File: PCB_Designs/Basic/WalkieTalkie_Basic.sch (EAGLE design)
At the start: 35 parts, among them Q1 MOSFET-NCHANNELBSS123LT1G, U1 ATMEGA328P

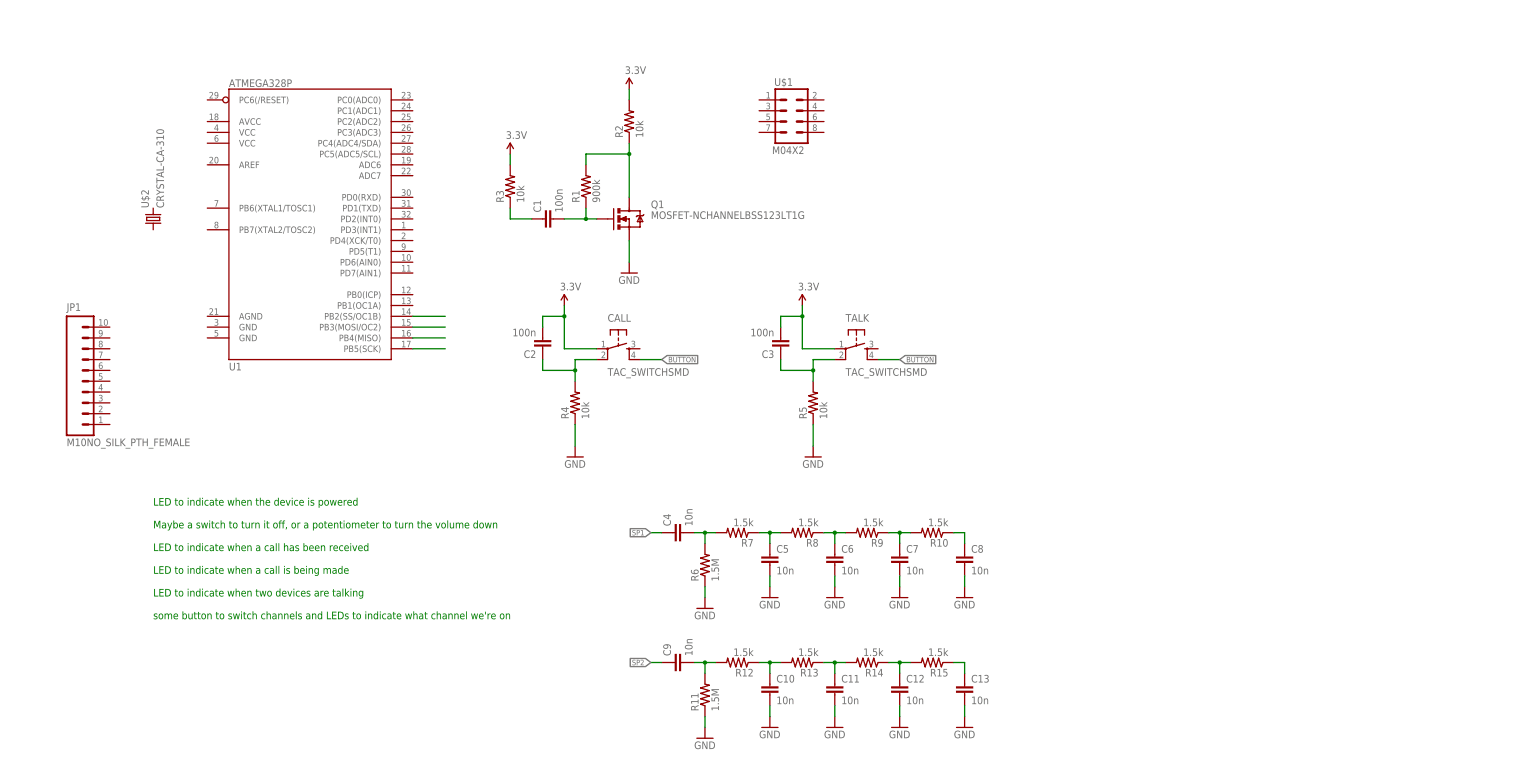
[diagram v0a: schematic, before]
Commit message: updating pcb design with labels, removed extra button, added library part for nRF24L01 breakout, etc
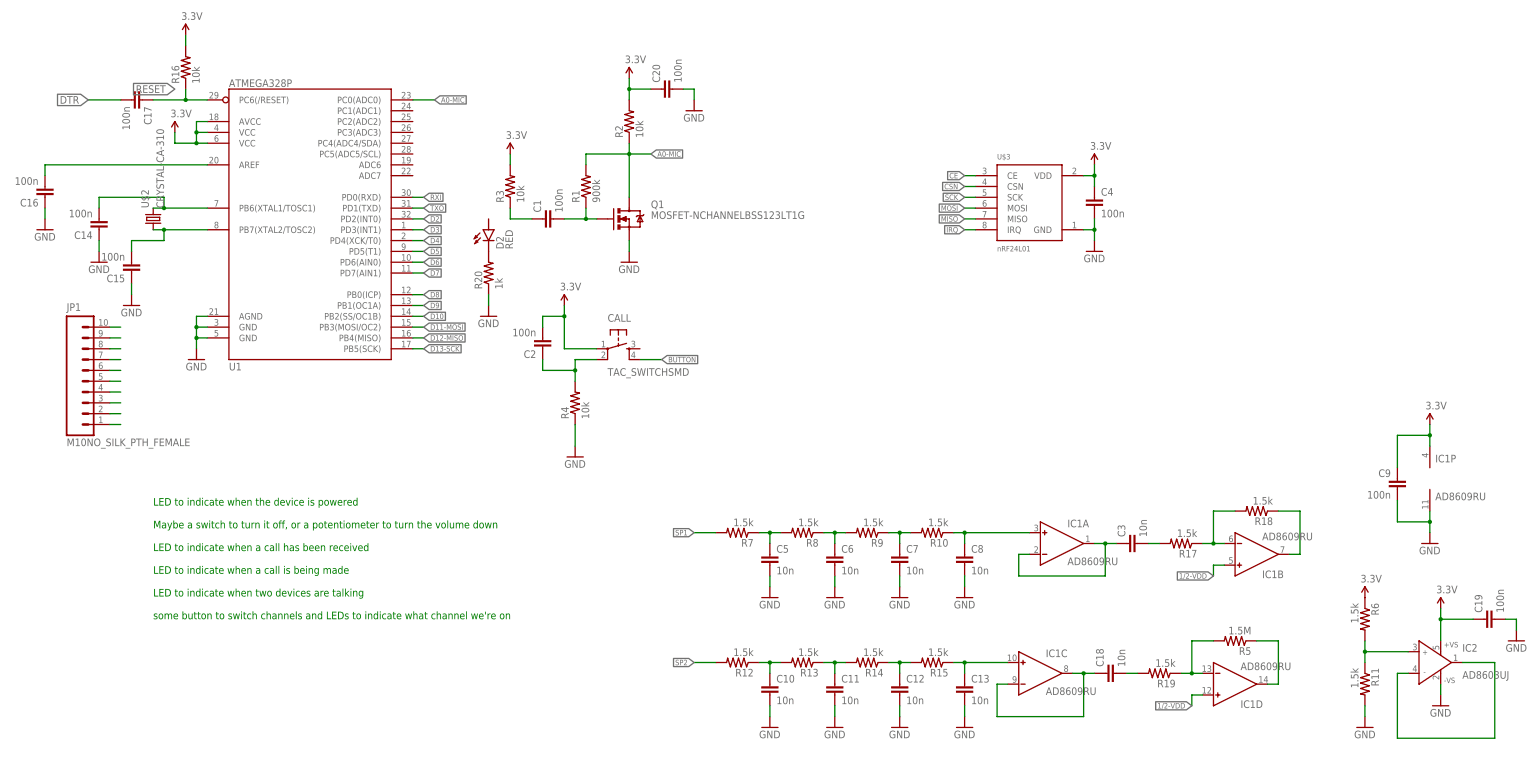
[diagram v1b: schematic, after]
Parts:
- removed TALK: TAC_SWITCHSMD, SparkFun-Retired:TAC_SWITCHSMD
- removed U$1: M04X2, SparkFun-Connectors:M04X2
- added C14, C15, C16, C17, C19, C20: 100n, resistor:C-EUC0402
- added C18: 10n, resistor:C-EUC0402
- added D2: RED, SparkFun-LED:LED-RED0603
- added IC1: AD8609RU, analog-devices:AD8609RU
- added IC2: AD8603UJ, analog-devices:AD8603UJ
- added R16: 10k, resistor:R-US_R0402
- added R17, R18, R19: 1.5k, resistor:R-US_R0402
- added R20: 1k, resistor:R-US_R0402
- added U$3: NRF24L01-BREAKOUT, Orlando:NRF24L01-BREAKOUT
- C3: value 100n -> 10n
- C4, C9: value 10n -> 100n
- R11, R6: value 1.5M -> 1.5k
- R5: value 10k -> 1.5M
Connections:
- net N$1 renamed D13-SCK
- net N$2 renamed D12-MISO
- net N$3 renamed D11-MOSI
- net N$4 renamed D10
- removed net N$15: C9.2, R11.2, R12.2
- new net 1/2-VDD: IC1B.IN+, IC1D.IN+, IC2.IN-, IC2.OUT
- new net A0-MIC: Q1.D, R1.2, R2.1, U1.PC0(ADC0)
- new net CE: U$3.CE
- new net CSN: U$3.CSN
- new net D2: U1.PD2(INT0)
- new net D3: U1.PD3(INT1)
- new net D4: U1.PD4(XCK/T0)
- new net D5: U1.PD5(T1)
- new net D6: U1.PD6(AIN0)
- new net D7: U1.PD7(AIN1)
- new net D8: U1.PB0(ICP)
- new net D9: U1.PB1(OC1A)
- new net DTR: C17.2
- new net IRQ: U$3.IRQ
- new net MISO: U$3.MISO
- new net MOSI: U$3.MOSI
- new net N$20: C14.2, U$2.2, U1.PB6(XTAL1/TOSC1)
- new net N$21: C15.2, U$2.1, U1.PB7(XTAL2/TOSC2)
- new net N$22: C16.2, U1.AREF
- new net N$23: C3.2, R17.2
- new net N$24: IC1B.IN-, R17.1, R18.2
- new net N$25: IC1B.OUT, R18.1
- new net N$26: C18.1, IC1C.IN-, IC1C.OUT
- new net N$27: IC1D.IN-, R19.1, R5.2
- new net N$28: C18.2, R19.2
- new net N$29: IC1D.OUT, R5.1
- new net N$37: JP1.10
- new net N$38: JP1.9
- new net N$39: JP1.8
- new net N$40: JP1.7
- new net N$41: JP1.6
- new net N$42: JP1.5
- new net N$43: JP1.4
- new net N$44: JP1.3
- new net N$45: JP1.2
- new net N$46: JP1.1
- new net RESET: C17.1, R16.1, U1.PC6(/RESET)
- new net RXI: U1.PD0(RXD)
- new net SCK: U$3.SCK
- new net TXO: U1.PD1(TXD)
- net 3.3V: now also C19.1, C20.1, C4.1, C9.1, IC1P.V+, IC2.+VS, R16.2, R6.1, U$3.VDD, U1.AVCC, U1.VCC@1, U1.VCC@2; no longer C3.2, TALK.1
- net BUTTON: no longer TALK.4
- net GND: now also C14.1, C15.1, C16.1, C19.2, C20.2, C4.2, C9.2, IC1P.V-, IC2.-VS, R11.2, R20.1, U$3.GND, U1.AGND, U1.GND@1, U1.GND@2; no longer R11.1, R5.1, R6.1
- net N$13: now also IC1A.IN+
- net N$18: now also IC1C.IN+
- net N$6: now also D2.C, R20.2; no longer Q1.D, R1.2, R2.1
- net N$7: now also IC1A.IN-, IC1A.OUT; no longer R5.2, TALK.2
- net N$9: now also IC2.IN+, R11.1; no longer C4.2, R7.2
- net SP1: now also R7.2; no longer C4.1
- net SP2: now also R12.2; no longer C9.1
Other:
- moved on the sheet: C3, C4, C9, R11, R5, R6

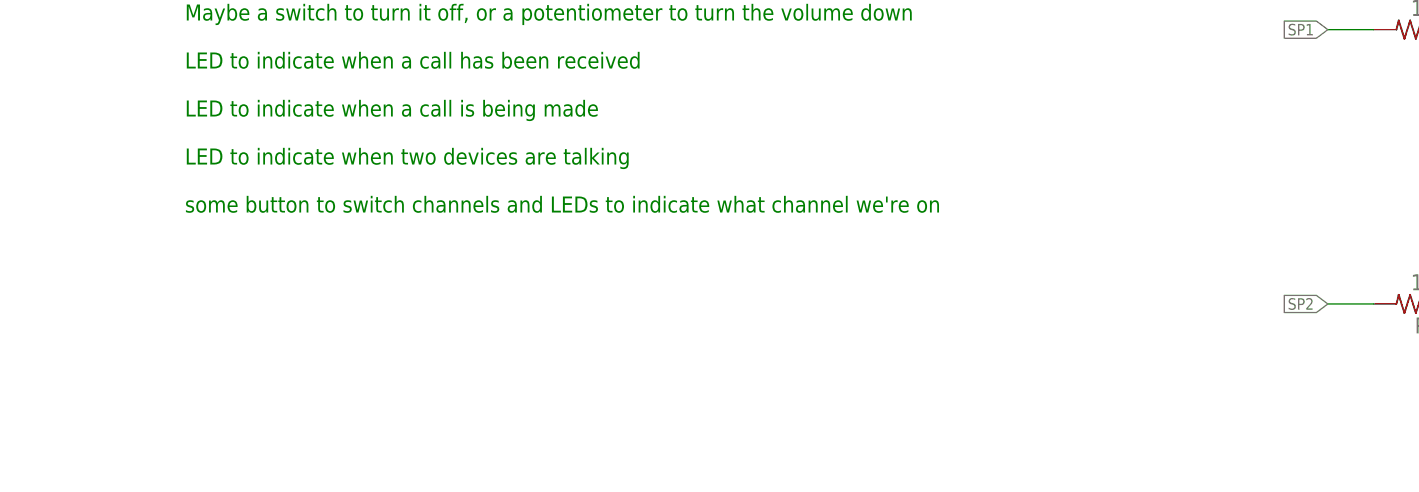
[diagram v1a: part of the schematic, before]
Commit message: added a reminder to add volume control to PCB design
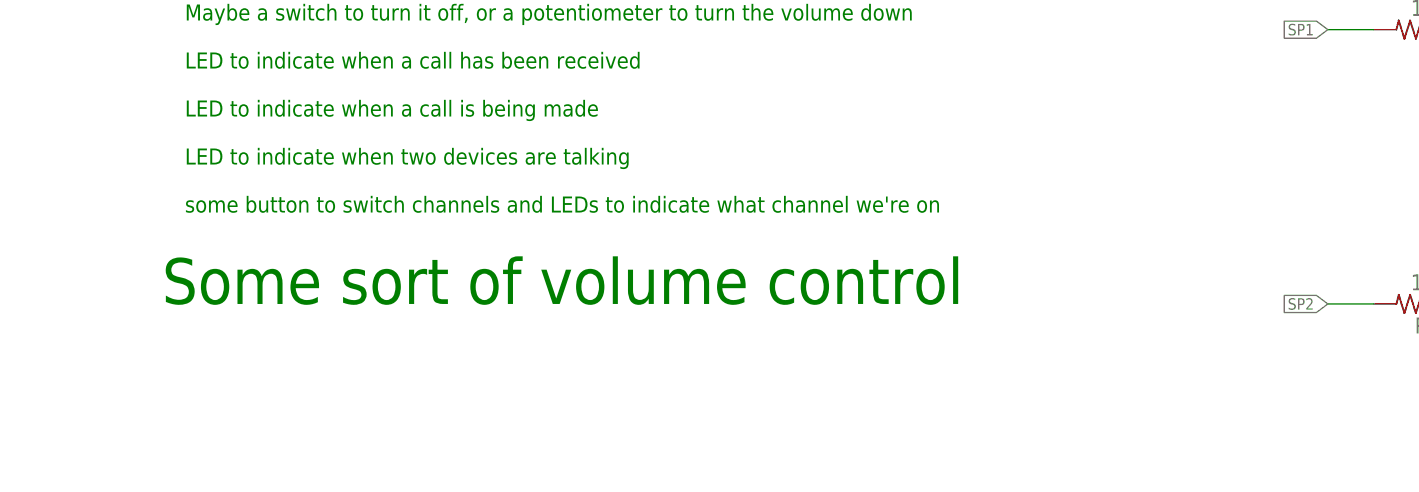
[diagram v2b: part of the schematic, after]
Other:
- note added: "Some sort of volume control"
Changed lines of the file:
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@@
 LED to indicate when two devices are talking
 some button to switch channels and LEDs to indicate what channel we're on</text>
+<text x="-10.16" y="-63.5" size="5.08" layer="91">Some sort of volume control</text>
 </plain>
 <instances>

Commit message: updating PCB design with buttons, LED indicators, etc.
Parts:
- added C21, C22: 100n, resistor:C-EUC0402
- added IC3: MCP601OT, linear:MCP601OT
- added R21: 10k, resistor:R-US_R0402
- added TALK: TAC_SWITCHSMD, SparkFun-Retired:TAC_SWITCHSMD
- added U$1: AUDIO-JACK3, SparkFun-Connectors:AUDIO-JACK3
- added U$4: AP2120N, OrlandoRonMod:AP2120N
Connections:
- removed net BUTTON: CALL.4
- removed net N$25: IC1B.OUT, R18.1
- removed net N$29: IC1D.OUT, R5.1
- new net N$1: C21.2, CALL.1, R21.2
- new net N$15: U$1.EARTH-GND/MIC
- new net N$2: C2.2, R4.2, TALK.1
- new net N$3: IC1B.OUT, R18.1, U$1.RIGHT
- new net N$4: IC1D.OUT, R5.1, U$1.LEFT
- new net TALK/CALL: CALL.4, TALK.4, U1.PC1(ADC1)
- net 3.3V: now also C22.1, IC3.V-, R21.1, R4.1; no longer C2.2, CALL.1
- net D3: now also IC3.-IN, IC3.OUT
- net D6: now also D2.A, IC3.+IN
- net GND: now also C2.1, C21.1, C22.2, CALL.2, IC3.V+, TALK.2; no longer R4.1
- net N$12: now also U$1.GND/MIC; no longer C2.1, CALL.2, R4.2
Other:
- moved on the sheet: C1, C19, C2, C20, C4, C9, CALL, D2, IC1P, IC2, Q1, R1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

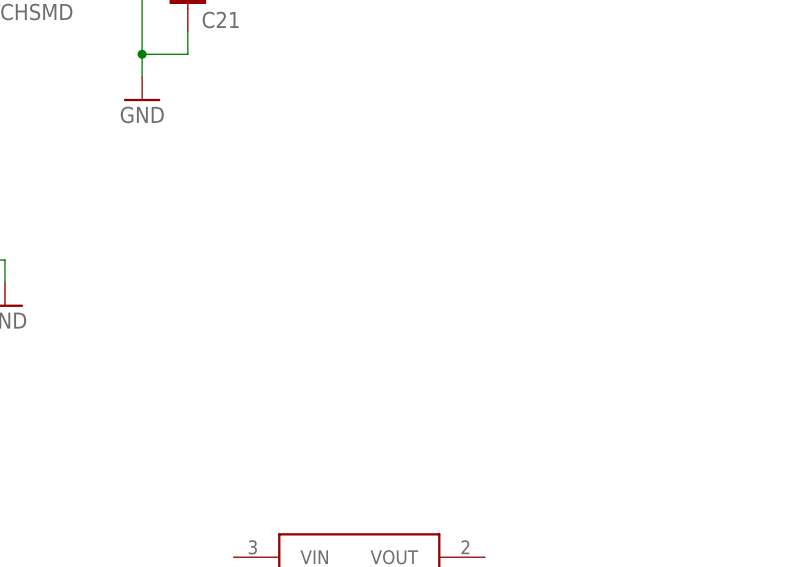
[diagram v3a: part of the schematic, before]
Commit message: updating PCB design and adding more datasheets
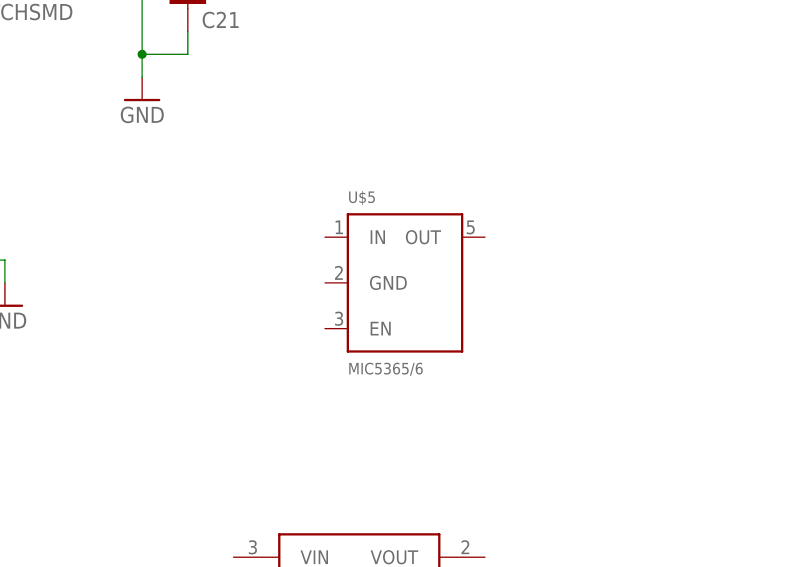
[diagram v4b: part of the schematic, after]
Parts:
- added U$5: MIC5365/6, Orlando:MIC5365/6
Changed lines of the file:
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@@
 <part name="U$1" library="SparkFun-Connectors" deviceset="AUDIO-JACK3" device=""/>
 <part name="U$4" library="OrlandoRonMod" deviceset="AP2120N" device=""/>
+<part name="U$5" library="Orlando" deviceset="MIC5365/6" device=""/>
 </parts>
 <sheets>
@@
 <instance part="U$1" gate="G$1" x="281.94" y="-48.26" rot="MR0"/>
 <instance part="U$4" gate="G$1" x="165.1" y="17.78"/>
+<instance part="U$5" gate="G$1" x="172.72" y="48.26"/>
 </instances>
 <busses>

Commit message: more PCB updates and more datasheets
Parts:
- removed C16: 100n, resistor:C-EUC0402
- removed JP1: M10NO_SILK_PTH_FEMALE, SparkFun-Connectors:M10NO_SILK_PTH_FEMALE
- removed U$5: MIC5365/6, Orlando:MIC5365/6
- added C23, C24: 100n, resistor:C-EUC0402
- added LDO: MIC5365/6, Orlando:MIC5365/6
- added MIC: MIC_CMC-5042PF-AC, Orlando:MIC_CMC-5042PF-AC
- added PROGRAM/BOOTLOAD: M10NO_SILK_PTH_FEMALE, SparkFun-Connectors:M10NO_SILK_PTH_FEMALE
- added XTAL: CRYSTAL-CA-310, OrlandoRonMod:CRYSTAL-CA-310
- U$2: value CRYSTAL-CA-310 -> PS1240P02CT3P; device OrlandoRonMod:CRYSTAL-CA-310 -> Orlando:PS1240P02CT3P
- U$4: value AP2120N -> BATT-CONNECT; device OrlandoRonMod:AP2120N -> OrlandoRonMod:BATT-CONNECT
- renumbered U1 to ARDUINO
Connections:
- removed net CE: U$3.CE
- removed net CSN: U$3.CSN
- removed net D10: ARDUINO.PB2(SS/OC1B)
- removed net D2: ARDUINO.PD2(INT0)
- removed net D7: ARDUINO.PD7(AIN1)
- removed net D8: ARDUINO.PB0(ICP)
- removed net D9: ARDUINO.PB1(OC1A)
- removed net IRQ: U$3.IRQ
- removed net MISO: U$3.MISO
- removed net MOSI: U$3.MOSI
- removed net N$22: ARDUINO.AREF, C16.2
- removed net N$37: JP1.10
- removed net N$38: JP1.9
- removed net N$39: JP1.8
- removed net N$40: JP1.7
- removed net N$41: JP1.6
- removed net N$42: JP1.5
- removed net N$43: JP1.4
- removed net N$44: JP1.3
- removed net N$45: JP1.2
- removed net N$46: JP1.1
- removed net SCK: U$3.SCK
- removed net SP1: R7.2
- removed net SP2: R12.2
- new net D10-SPEAK2: ARDUINO.PB2(SS/OC1B), R12.2
- new net D2-IRQ: ARDUINO.PD2(INT0), U$3.IRQ
- new net D7-CE: ARDUINO.PD7(AIN1), U$3.CE
- new net D8-CSN: ARDUINO.PB0(ICP), U$3.CSN
- new net D9-SPEAK1: ARDUINO.PB1(OC1A), R7.2
- new net V_BATT: C23.1, LDO.EN, LDO.IN, U$4G$2.TP
- net 3.3V: now also C24.1, LDO.OUT, PROGRAM/BOOTLOAD.8
- net D11-MOSI: now also PROGRAM/BOOTLOAD.3, U$3.MOSI
- net D12-MISO: now also PROGRAM/BOOTLOAD.2, U$3.MISO
- net D13-SCK: now also PROGRAM/BOOTLOAD.1, U$3.SCK
- net D3: now also U$2.+
- net D6: now also R20.2; no longer D2.A
- net DTR: now also PROGRAM/BOOTLOAD.5
- net GND: now also C23.2, C24.2, D2.C, LDO.GND, MIC.-, PROGRAM/BOOTLOAD.10, PROGRAM/BOOTLOAD.9, U$2.-, U$4G$1.TP; no longer C16.1, R20.1
- net N$20: now also XTAL.2; no longer U$2.2
- net N$21: now also XTAL.1; no longer U$2.1
- net N$6: now also D2.A, R20.1; no longer D2.C, R20.2
- net N$8: now also MIC.+
- net RESET: now also PROGRAM/BOOTLOAD.4
- net RXI: now also PROGRAM/BOOTLOAD.7
- net TXO: now also PROGRAM/BOOTLOAD.6
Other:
- moved on the sheet: C15, C4, D2, R20, U$3

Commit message: updates to PCB
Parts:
- C14, C15: value 100n -> 22p
- renumbered U$4 to LIPO
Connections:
- net 1/2-VDD: now also IC1C.IN+; no longer IC1B.IN+
- net D10-SPEAK2: now also R7.2; no longer R12.2
- net D9-SPEAK1: now also R12.2; no longer R7.2
- net N$18: now also IC1B.IN+; no longer IC1C.IN+
- net N$24: now also IC1D.IN-; no longer IC1B.IN-
- net N$26: now also IC1B.IN-, IC1B.OUT; no longer IC1C.IN-, IC1C.OUT
- net N$27: now also IC1C.IN-; no longer IC1D.IN-
- net N$3: now also IC1D.OUT; no longer IC1B.OUT
- net N$4: now also IC1C.OUT; no longer IC1D.OUT
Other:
- moved on the sheet: C4, IC1B, IC1C, IC1D

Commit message: more updates to PCB almost done
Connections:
- new net N$22: ARDUINO.PC2(ADC2)
- new net N$25: ARDUINO.PC3(ADC3)
- new net N$29: ARDUINO.PC4(ADC4/SDA)
- new net N$30: ARDUINO.PC5(ADC5/SCL)
- new net N$31: ARDUINO.ADC6
- new net N$32: ARDUINO.ADC7
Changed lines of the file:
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@@
 <?xml version="1.0" encoding="utf-8"?>
 <!DOCTYPE eagle SYSTEM "eagle.dtd">
-<eagle version="7.4.0">
+<eagle version="7.3.0">
 <drawing>
 <settings>
@@
 </segment>
 </net>
+<net name="N$22" class="0">
+<segment>
+<pinref part="ARDUINO" gate="G$1" pin="PC2(ADC2)"/>
+<wire x1="53.34" y1="63.5" x2="55.88" y2="63.5" width="0.1524" layer="91"/>
+</segment>
+</net>
+<net name="N$25" class="0">
+<segment>
+<pinref part="ARDUINO" gate="G$1" pin="PC3(ADC3)"/>
+<wire x1="53.34" y1="60.96" x2="55.88" y2="60.96" width="0.1524" layer="91"/>
+</segment>
+</net>
+<net name="N$29" class="0">
+<segment>
+<pinref part="ARDUINO" gate="G$1" pin="PC4(ADC4/SDA)"/>
+<wire x1="53.34" y1="58.42" x2="55.88" y2="58.42" width="0.1524" layer="91"/>
+</segment>
+</net>
+<net name="N$30" class="0">
+<segment>
+<pinref part="ARDUINO" gate="G$1" pin="PC5(ADC5/SCL)"/>
+<wire x1="53.34" y1="55.88" x2="55.88" y2="55.88" width="0.1524" layer="91"/>
+</segment>
+</net>
+<net name="N$31" class="0">
+<segment>
+<pinref part="ARDUINO" gate="G$1" pin="ADC6"/>
+<wire x1="53.34" y1="53.34" x2="55.88" y2="53.34" width="0.1524" layer="91"/>
+</segment>
+</net>
+<net name="N$32" class="0">
+<segment>
+<pinref part="ARDUINO" gate="G$1" pin="ADC7"/>
+<wire x1="53.34" y1="50.8" x2="55.88" y2="50.8" width="0.1524" layer="91"/>
+</segment>
+</net>

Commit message: more updates almost done
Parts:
- added S1: TAC_SWITCHSMD, SparkFun-Retired:TAC_SWITCHSMD
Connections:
- new net N$34: CALL.3
- net GND: now also CALL.4, TALK.4; no longer CALL.2, TALK.2
- net N$1: now also TALK.2; no longer C21.2, CALL.1, R21.2
- net N$2: now also TALK.3; no longer C2.2, R4.2, TALK.1
- net TALK/CALL: now also C2.2, C21.2, CALL.1, R21.2, R4.2, TALK.1; no longer CALL.4, TALK.4
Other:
- moved on the sheet: C2, C21, C23, C24, LDO, LIPOG$1, LIPOG$2, R4, TALK
